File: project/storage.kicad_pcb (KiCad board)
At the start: 6 copper layers, 190 x 134 mm, 53 parts

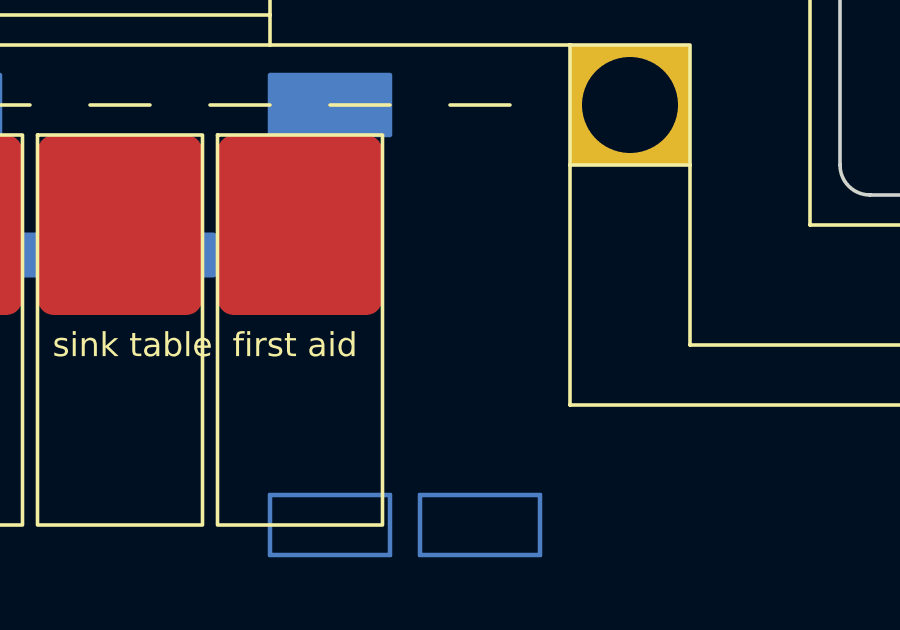
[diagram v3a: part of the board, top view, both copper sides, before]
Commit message: small tweeks and fixes as we implement the plan
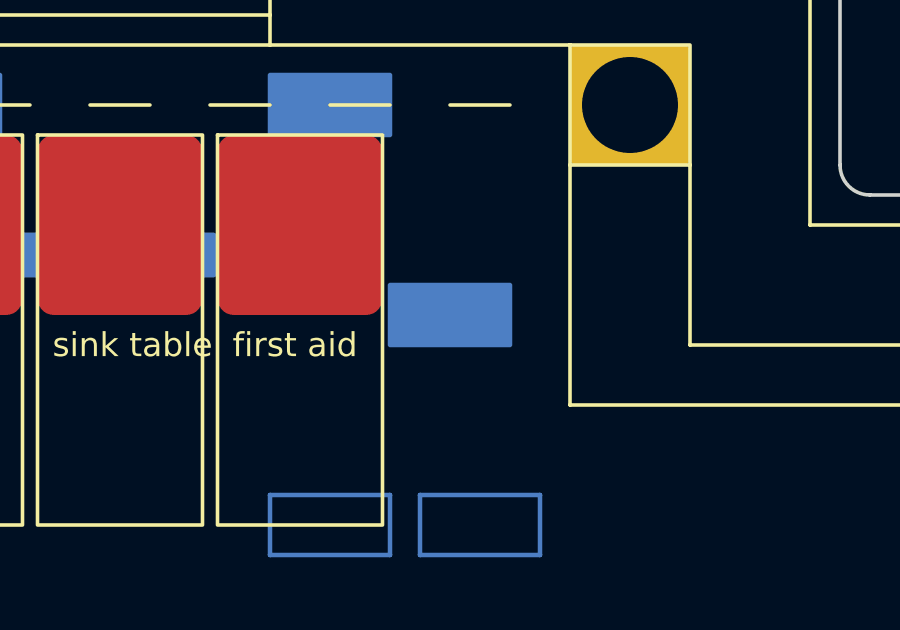
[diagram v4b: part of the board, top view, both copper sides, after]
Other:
- board text added: "3x1 108m for room 8 lights"
- board text added: "3x1 15m for room 6 lights"
- board text added: "3x1 5m for room 7 lights"
- board text added: "3x2.5 15m via D821 x3"
- board text added: "3x2.5 8m via D821 x3"
- board text added: "3x2.5 C16 28m x1 boiler"
- board text added: "3x2.5 C16 32m x3"
- board text added: "D712"
- board text removed: "3x2.5 15m via D821 x4"
- board text removed: "3x2.5 8m via D821 x4"
- board text removed: "3x2.5 C16 32m x6"
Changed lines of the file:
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@@
       (effects (font (size 1 1) (thickness 0.15)))
     )
-    (fp_text user "h=2.34" (at 84 10 unlocked) (layer "User.1")
+    (fp_text user "h=2.34" (at 83 7 unlocked) (layer "User.1")
       (effects (font (size 1 1) (thickness 0.15)))
     )
@@
     ) (layer "B.Cu") (width 0.15) (fill solid))
   (gr_rect (start 210 146) (end 214 144) (layer "B.Cu") (width 0.15) (fill none))
+  (gr_rect (start 169 39) (end 173 41) (layer "B.Cu") (width 0.15) (fill solid))
   (gr_rect (start 228 61) (end 232 59) (layer "B.Cu") (width 0.15) (fill none))
   (gr_rect (start 63 91) (end 67 89) (layer "B.Cu") (width 0.15) (fill none))
@@
   (gr_line (start 108.5 49.5) (end 109.5 48.5) (layer "User.3") (width 0.15))
   (gr_line (start 172 56) (end 172 50) (layer "User.3") (width 0.15))
+  (gr_line (start 167 42) (end 167 41) (layer "User.3") (width 0.15))
   (gr_line (start 226 40) (end 226 39) (layer "User.3") (width 0.15))
   (gr_line (start 86 161.5) (end 87 160.5) (layer "User.3") (width 0.15))
@@
   (gr_line (start 48 56) (end 49 57) (layer "User.3") (width 0.15))
   (gr_line (start 109.5 49.5) (end 108.5 49.5) (layer "User.3") (width 0.15))
+  (gr_line (start 167 40) (end 168 41) (layer "User.3") (width 0.15))
   (gr_line (start 65 93) (end 64 93) (layer "User.3") (width 0.15))
   (gr_line (start 109.5 48.5) (end 110.5 49.5) (layer "User.3") (width 0.15))
@@
   (gr_line (start 227 40) (end 226 41) (layer "User.3") (width 0.15))
   (gr_line (start 205 47) (end 204 47) (layer "User.3") (width 0.15))
+  (gr_line (start 168 41) (end 167 42) (layer "User.3") (width 0.15))
   (gr_line (start 90 92) (end 91 93) (layer "User.3") (width 0.15))
   (gr_line (start 64 99) (end 64 93) (layer "User.3") (width 0.15))
@@
   (gr_line (start 89 36) (end 89 43) (layer "User.3") (width 0.15))
   (gr_line (start 64 92) (end 65 93) (layer "User.3") (width 0.15))
+  (gr_line (start 162 41) (end 167 41) (layer "User.3") (width 0.15))
   (gr_line (start 171 50) (end 172 49) (layer "User.3") (width 0.15))
   (gr_line (start 89 93) (end 90 92) (layer "User.3") (width 0.15))
@@
   (gr_line (start 48 45) (end 48 44) (layer "User.3") (width 0.15))
   (gr_line (start 173 50) (end 172 50) (layer "User.3") (width 0.15))
+  (gr_line (start 167 41) (end 167 40) (layer "User.3") (width 0.15))
   (gr_line (start 226 41) (end 226 40) (layer "User.3") (width 0.15))
   (gr_line (start 226 56) (end 227 57) (layer "User.3") (width 0.15))
@@
     (effects (font (size 1 1) (thickness 0.15)) (justify left))
   )
+  (gr_text "3x1 108m for room 8 lights" (at 127 143) (layer "User.3")
+    (effects (font (size 2 2) (thickness 0.3)) (justify left))
+  )
   (gr_text "45" (at 57 89) (layer "User.3")
     (effects (font (size 1 1) (thickness 0.15)) (justify left))
   )
-  (gr_text "3x2.5 15m\nvia D821 x4" (at 86 165) (layer "User.3")
+  (gr_text "3x2.5 15m\nvia D821 x3" (at 86 165) (layer "User.3")
     (effects (font (size 2 2) (thickness 0.3)) (justify right))
   )
@@
     (effects (font (size 1 1) (thickness 0.15)) (justify left))
   )
-  (gr_text "3x2.5 C16\n32m x6" (at 167 20) (layer "User.3")
+  (gr_text "3x2.5 C16\n32m x3" (at 167 20) (layer "User.3")
     (effects (font (size 2 2) (thickness 0.3)) (justify left))
   )
@@
     (effects (font (size 1 1) (thickness 0.15)) (justify left))
   )
+  (gr_text "3x2.5 C16 28m x1 boiler" (at 128 43) (layer "User.3")
+    (effects (font (size 2 2) (thickness 0.3)) (justify left))
+  )
   (gr_text "D85K" (at 113 103 90) (layer "User.3")
     (effects (font (size 1 1) (thickness 0.15)) (justify left))
+  )
+  (gr_text "3x1 5m for room 7 lights" (at 127 133) (layer "User.3")
+    (effects (font (size 2 2) (thickness 0.3)) (justify left))
   )
   (gr_text "D85G" (at 95 45) (layer "User.3")
@@
     (effects (font (size 1 1) (thickness 0.15)) (justify left))
   )
+  (gr_text "3x1 15m for room 6 lights" (at 127 123) (layer "User.3")
+    (effects (font (size 2 2) (thickness 0.3)) (justify left))
+  )
   (gr_text "D85B" (at 87 118 90) (layer "User.3")
     (effects (font (size 1 1) (thickness 0.15)) (justify left))
@@
     (effects (font (size 1 1) (thickness 0.15)) (justify left))
   )
-  (gr_text "3x2.5 8m\nvia D821 x4" (at 43 57) (layer "User.3")
+  (gr_text "3x2.5 8m\nvia D821 x3" (at 43 57) (layer "User.3")
     (effects (font (size 2 2) (thickness 0.3)) (justify right))
   )
@@
     (effects (font (size 1 1) (thickness 0.15)) (justify left))
   )
+  (gr_text "D712" (at 169 40) (layer "User.3")
+    (effects (font (size 1 1) (thickness 0.15)) (justify left))
+  )
   (gr_text "xx3x" (at 130 81) (layer "User.3")
     (effects (font (size 1 1) (thickness 0.15)))
@@
     (effects (font (size 1 1) (thickness 0.15)) (justify left))
   )
-  (gr_text "14" (at 171 41) (layer "User.4")
-    (effects (font (size 1 1) (thickness 0.15)) (justify left))
-  )
+  (gr_text "14" (at 175 42) (layer "User.4")
+    (effects (font (size 1 1) (thickness 0.15)) (justify left))
+  )

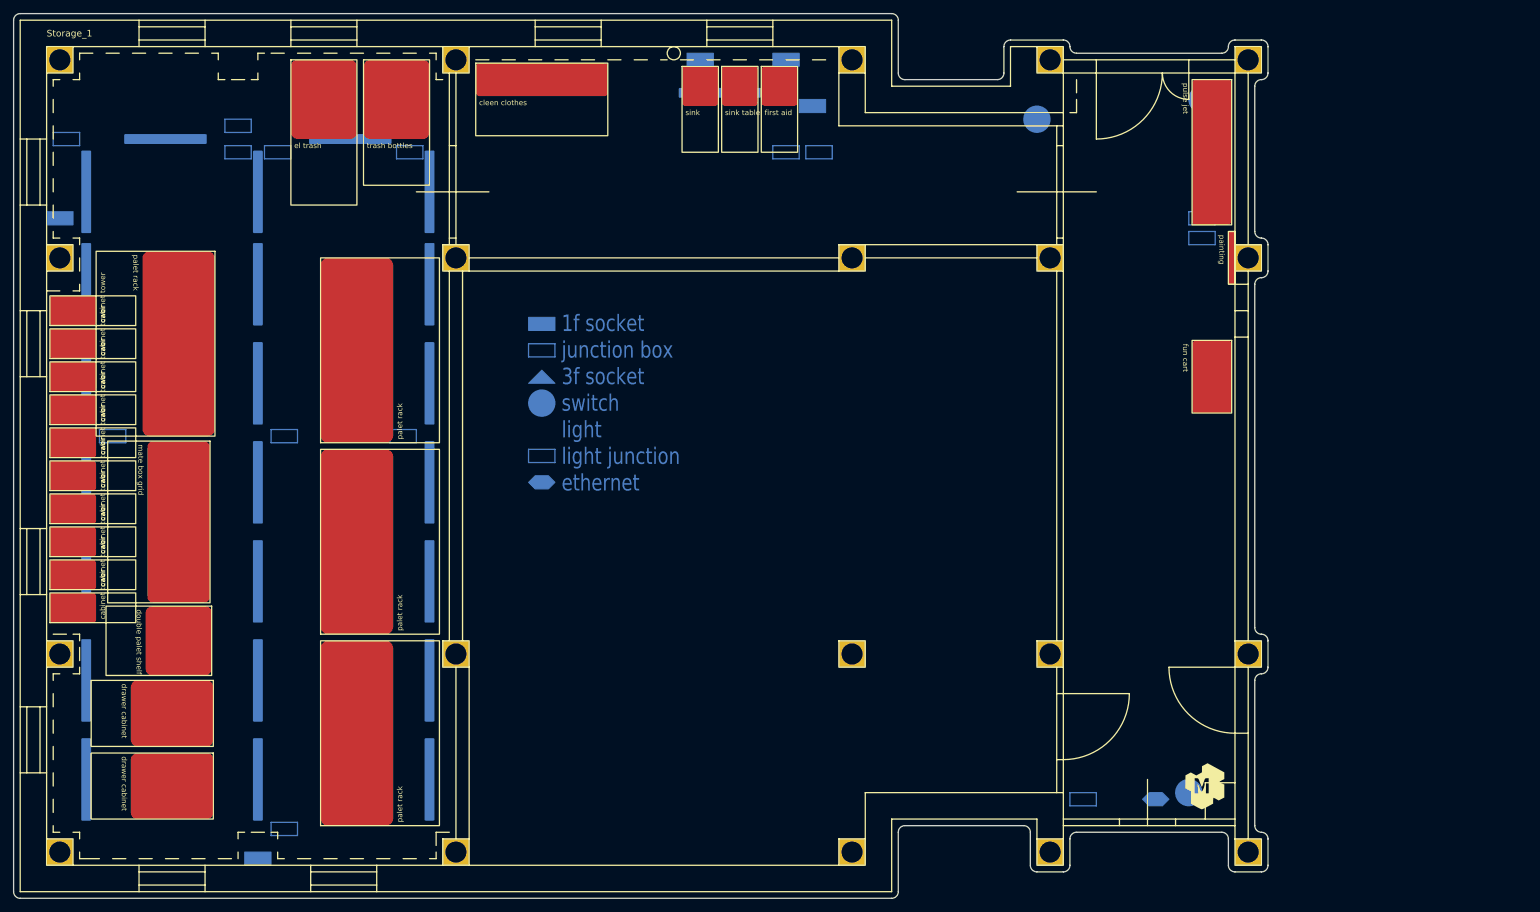
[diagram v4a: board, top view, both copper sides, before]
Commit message: adding comunications wiring and naming
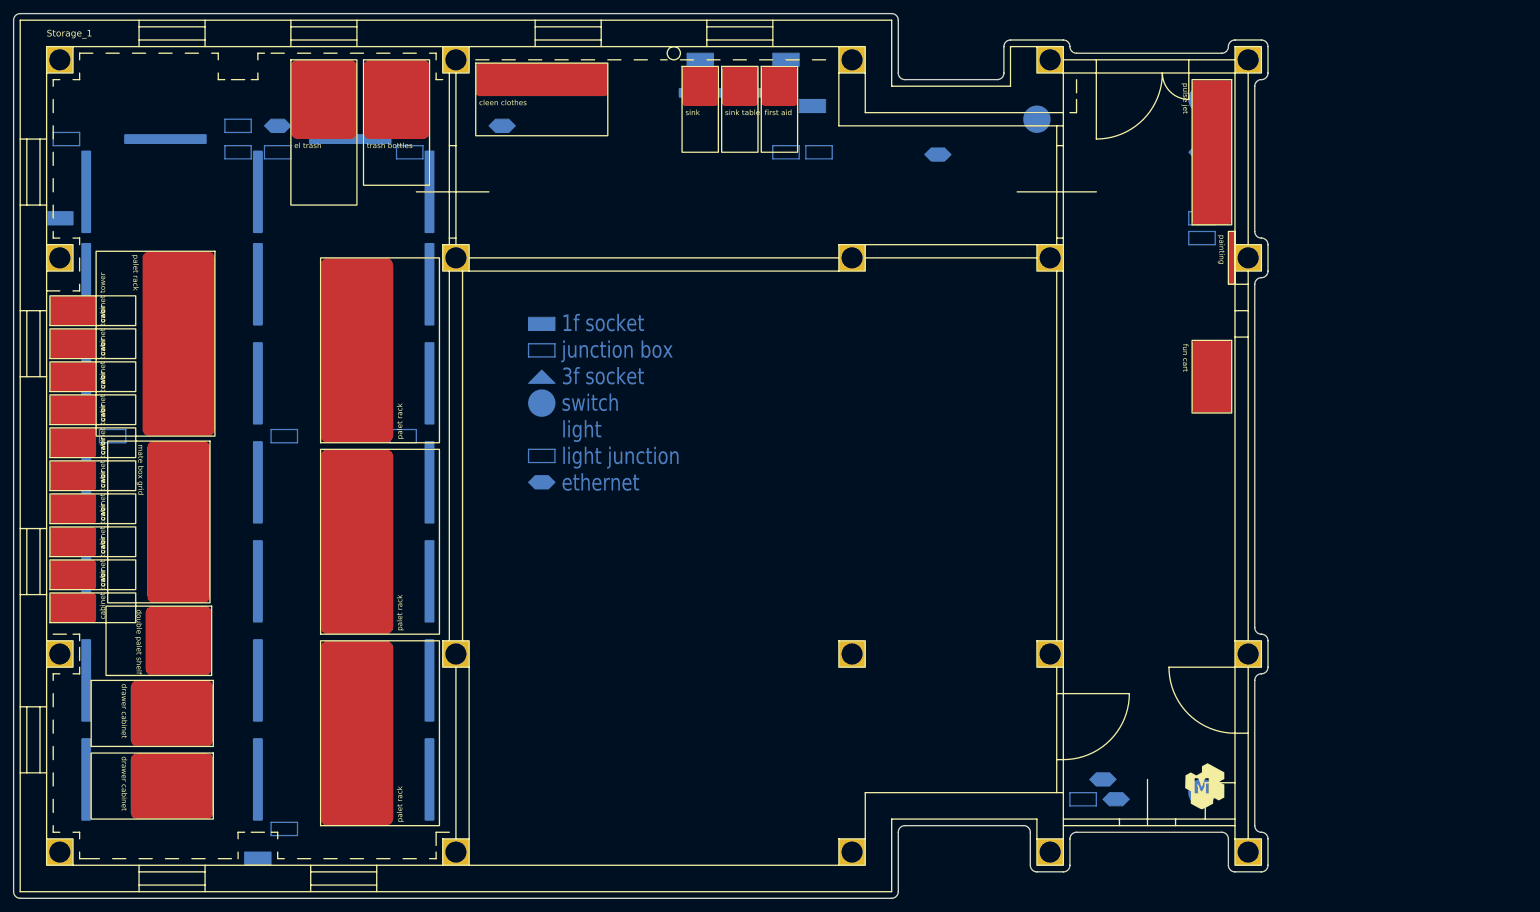
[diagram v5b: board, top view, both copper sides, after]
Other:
- board text added: "000"
- board text added: "25"
- board text added: "32"
- board text added: "36"
- board text added: "ap-L7 33m"
- board text added: "ap-S7 25m"
- board text added: "ap-S8 38m"
- board text added: "ap-U8 35m"
- board text added: "cam-iejimas 38m"
- board text added: "cam-koridirius 25m"
- board text added: "maglock 38m"
- board text removed: "101"
- board text removed: "38m"

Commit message: adding comunication cable numbers
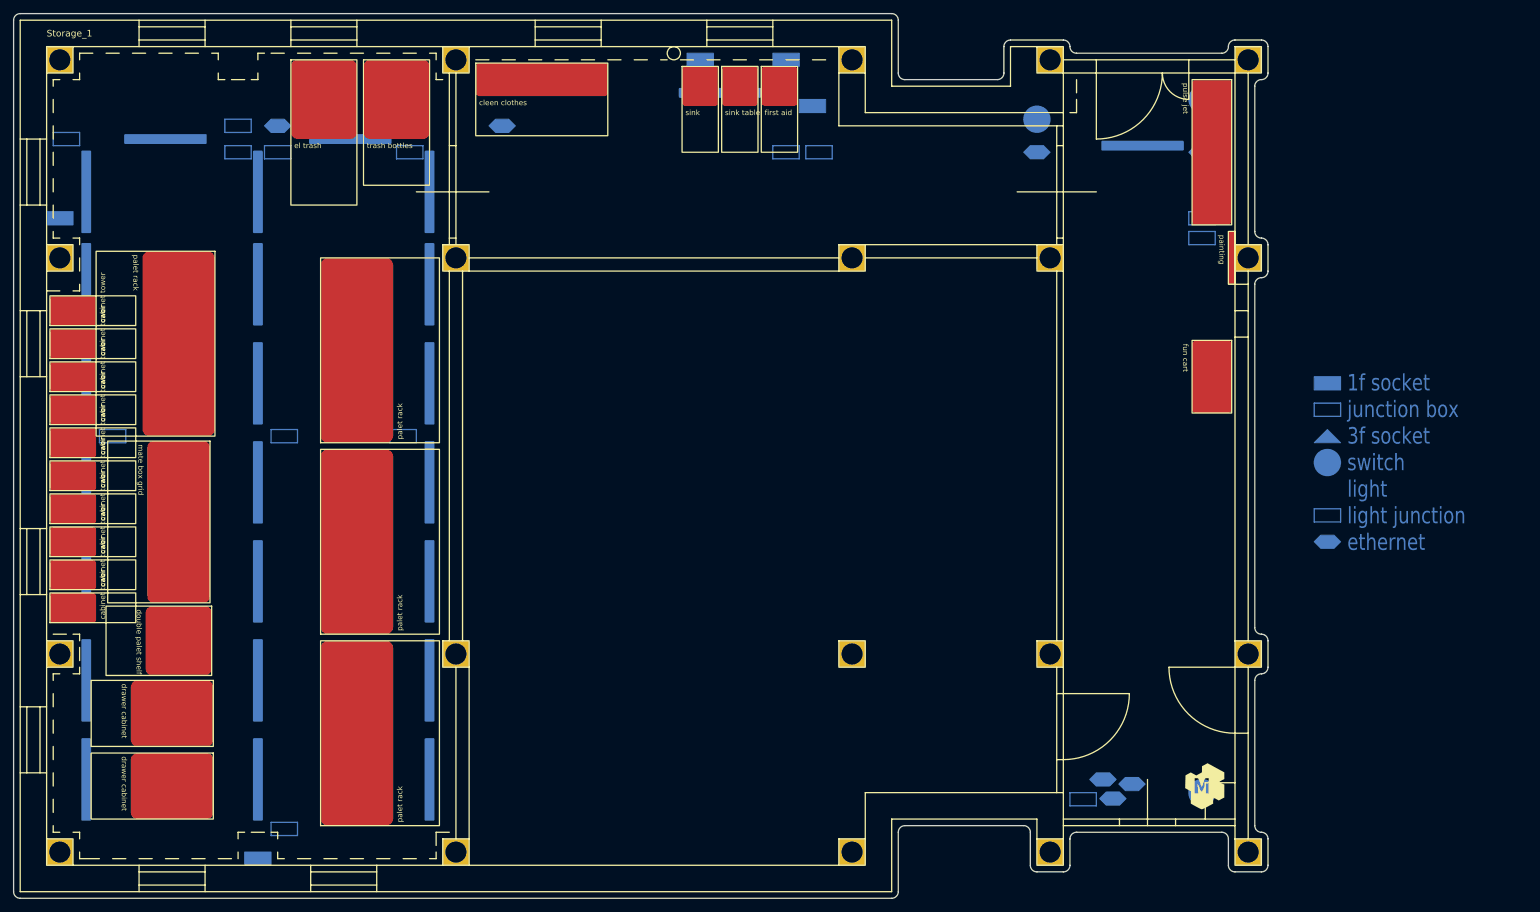
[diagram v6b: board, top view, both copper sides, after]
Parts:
- added L25: light, -local:light_long, B.Cu at (221.0, 46.0)
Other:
- board text added: "105"
- board text added: "109"
- board text added: "110"
- board text added: "113"
- board text added: "114"
- board text added: "116"
- board text added: "124"
- board text added: "D655-5"
- board text added: "ap-L6 38m"
- board text added: "cam-gate 38m"
- board text added: "cam-hallway1 25m"
- board text removed: "000"
- board text removed: "cam-iejimas 38m"
- board text removed: "cam-koridirius 25m"

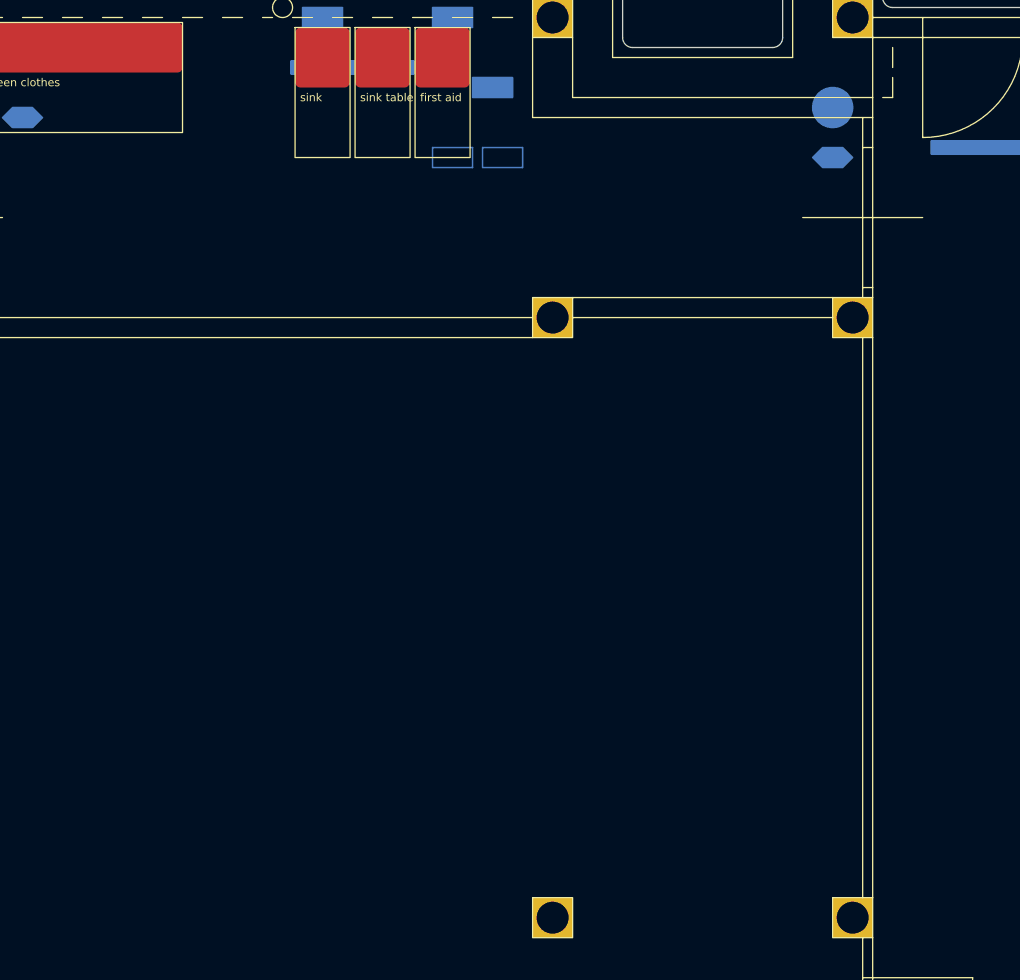
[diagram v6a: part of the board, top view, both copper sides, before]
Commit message: adding few light fixtured in storage area
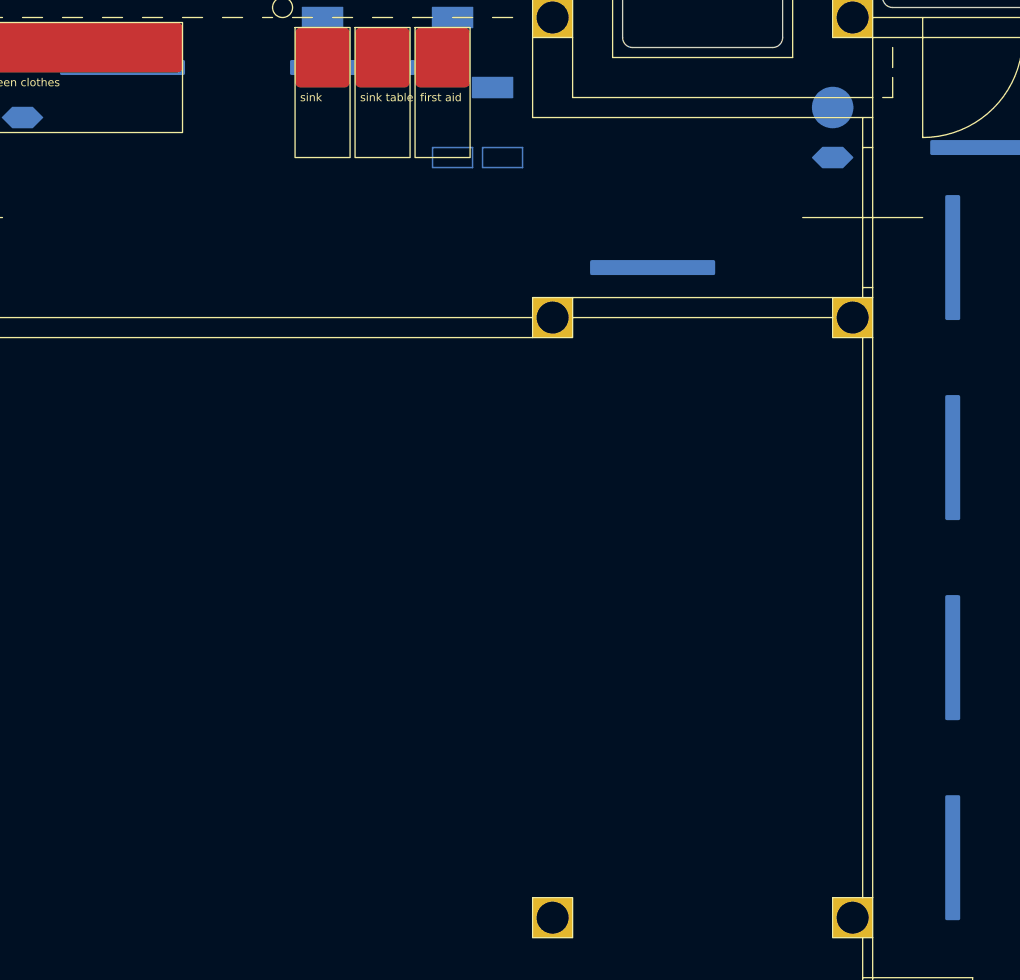
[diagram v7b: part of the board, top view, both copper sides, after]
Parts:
- added L26: light, -local:light_long, B.Cu at (217.0, 77.0)
- added L27: light, -local:light_long, B.Cu at (134.0, 38.0)
- added L28: light, -local:light_long, B.Cu at (217.0, 57.0)
- added L29: light, -local:light_long, B.Cu at (187.0, 58.0)
- added L30: light, -local:light_long, B.Cu at (217.0, 97.0)
- added L31: light, -local:light_long, B.Cu at (217.0, 117.0)
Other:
- board text added: "D651"
- board text added: "D652"
- board text added: "D653"
- board text added: "D654"
- board text added: "D655"
- board text added: "D752"
- board text added: "D753"
- board text removed: "D655-5"
